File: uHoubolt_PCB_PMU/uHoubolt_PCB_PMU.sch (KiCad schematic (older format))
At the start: 43 parts, among them J1 Conn_01x04, J2 Conn_01x02, J3 Conn_01x04, Q1 BUK7M27-80EX, Q2 Si7141DP, SW1 SW_Push_SPDT, SW2 SW_Push_SPDT, U1 INA226, U2 MAX1873SEEE

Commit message: replace mosfet
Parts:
- removed Q1: BUK7M27-80EX, Package_TO_SOT_SMD:LFPAK33, symbol Transistor_FET:BUK7M27-80EX
- added Q?: ZXMN3F30FH, Package_TO_SOT_SMD:SOT-23, symbol Transistor_FET:ZXMN3F30FH
- added R?: 200, symbol Device:R_Small
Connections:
- wire segments 149 -> 151
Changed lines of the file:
@@
 Wire Wire Line
 	6700 4350 6700 4500
-$Comp
-L power:GND #PWR016
-U 1 1 5FE435F1
-P 6700 4700
-F 0 "#PWR016" H 6700 4450 50  0001 C CNN
-F 1 "GND" H 6705 4527 50  0000 C CNN
-F 2 "" H 6700 4700 50  0001 C CNN
-F 3 "" H 6700 4700 50  0001 C CNN
-	1    6700 4700
-	1    0    0    -1
-$EndComp
 Wire Wire Line
 	6550 4000 6550 3800
@@
 	1    0    0    1
 $EndComp
-$Comp
-L Transistor_FET:BUK7M27-80EX Q1
-U 1 1 600D7062
-P 5950 3850
-F 0 "Q1" H 5650 3750 50  0000 L CNN
-F 1 "BUK7M27-80EX" H 5400 3650 50  0000 L CNN
-F 2 "Package_TO_SOT_SMD:LFPAK33" H 6150 3775 50  0001 L CIN
-F 3 "https://assets.nexperia.com/documents/data-sheet/BUK7M27-80E.pdf" V 5950 3850 50  0001 L CNN
-	1    5950 3850
-	1    0    0    -1
-$EndComp
-Text Label 5400 3850 0    50   ~ 0
+Text Label 5175 3850 0    50   ~ 0
 DISABLE
-Wire Wire Line
-	5400 3850 5750 3850
 Wire Wire Line
 	6050 3650 6700 3650
@@
 	6700 3650 6700 3700
 Connection ~ 6700 3700
-$Comp
-L power:GND #PWR013
-U 1 1 600E6257
-P 6050 4050
-F 0 "#PWR013" H 6050 3800 50  0001 C CNN
-F 1 "GND" H 6125 3875 50  0000 R CNN
-F 2 "" H 6050 4050 50  0001 C CNN
-F 3 "" H 6050 4050 50  0001 C CNN
-	1    6050 4050
-	1    0    0    -1
-$EndComp
 $Comp
 L Device:R_Small R14
@@
 Wire Wire Line
 	3400 5450 3000 5450
+$Comp
+L Transistor_FET:ZXMN3F30FH Q?
+U 1 1 5FF6F840
+P 5950 3850
+F 0 "Q?" H 6154 3896 50  0000 L CNN
+F 1 "ZXMN3F30FH" H 6154 3805 50  0000 L CNN
+F 2 "Package_TO_SOT_SMD:SOT-23" H 6150 3775 50  0001 L CIN
+F 3 "http://www.diodes.com/assets/Datasheets/ZXMN3F30FH.pdf" H 5950 3850 50  0001 L CNN
+	1    5950 3850
+	1    0    0    -1
+$EndComp
+$Comp
+L power:GND #PWR016
+U 1 1 5FE435F1
+P 6700 4700
+F 0 "#PWR016" H 6700 4450 50  0001 C CNN
+F 1 "GND" H 6705 4527 50  0000 C CNN
+F 2 "" H 6700 4700 50  0001 C CNN
+F 3 "" H 6700 4700 50  0001 C CNN
+	1    6700 4700
+	1    0    0    -1
+$EndComp
+$Comp
+L power:GND #PWR?
+U 1 1 5FF780F7
+P 6050 4100
+F 0 "#PWR?" H 6050 3850 50  0001 C CNN
+F 1 "GND" H 6055 3927 50  0000 C CNN
+F 2 "" H 6050 4100 50  0001 C CNN
+F 3 "" H 6050 4100 50  0001 C CNN
+	1    6050 4100
+	1    0    0    -1
+$EndComp
+Wire Wire Line
+	6050 4050 6050 4100
+$Comp
+L Device:R_Small R?
+U 1 1 5FF7FCD0
+P 5550 3850
+F 0 "R?" V 5625 3800 50  0000 L CNN
+F 1 "200" V 5675 3775 50  0000 L CNN
+F 2 "" H 5550 3850 50  0001 C CNN
+F 3 "~" H 5550 3850 50  0001 C CNN
+	1    5550 3850
+	0    1    1    0
+$EndComp
+Wire Wire Line
+	5650 3850 5750 3850
+Wire Wire Line
+	5450 3850 5175 3850
 $EndSCHEMATC

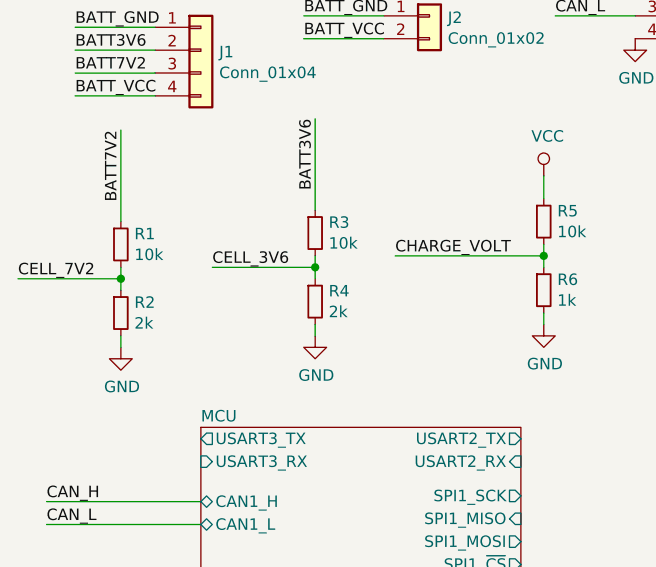
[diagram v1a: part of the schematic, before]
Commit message: change voltage divider values
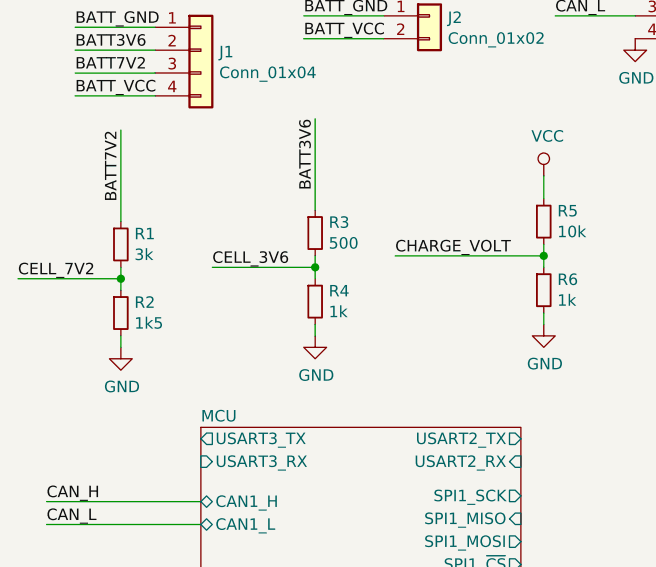
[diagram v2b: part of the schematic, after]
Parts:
- R1: value 10k -> 3k
- R2: value 2k -> 1k5
- R3: value 10k -> 500
- R4: value 2k -> 1k
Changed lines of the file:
@@
 AR Path="/5FE7A048" Ref="R3"  Part="1"
 F 0 "R3" H 2159 2946 50  0000 L CNN
-F 1 "10k" H 2159 2855 50  0000 L CNN
+F 1 "500" H 2159 2855 50  0000 L CNN
 F 2 "" H 2100 2900 50  0001 C CNN
 F 3 "~" H 2100 2900 50  0001 C CNN
@@
 AR Path="/5FE7A04E" Ref="R4"  Part="1"
 F 0 "R4" H 2159 3246 50  0000 L CNN
-F 1 "2k" H 2159 3155 50  0000 L CNN
+F 1 "1k" H 2159 3155 50  0000 L CNN
 F 2 "" H 2100 3200 50  0001 C CNN
 F 3 "~" H 2100 3200 50  0001 C CNN
@@
 AR Path="/5FE86386" Ref="R1"  Part="1"
 F 0 "R1" H 1309 2996 50  0000 L CNN
-F 1 "10k" H 1309 2905 50  0000 L CNN
+F 1 "3k" H 1309 2905 50  0000 L CNN
 F 2 "" H 1250 2950 50  0001 C CNN
 F 3 "~" H 1250 2950 50  0001 C CNN
@@
 AR Path="/5FE8638C" Ref="R2"  Part="1"
 F 0 "R2" H 1309 3296 50  0000 L CNN
-F 1 "2k" H 1309 3205 50  0000 L CNN
+F 1 "1k5" H 1309 3205 50  0000 L CNN
 F 2 "" H 1250 3250 50  0001 C CNN
 F 3 "~" H 1250 3250 50  0001 C CNN

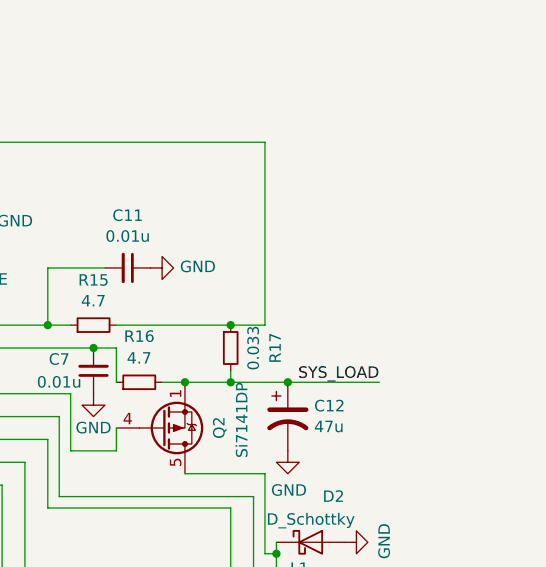
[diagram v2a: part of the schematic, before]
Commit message: add voltage divider sys_load
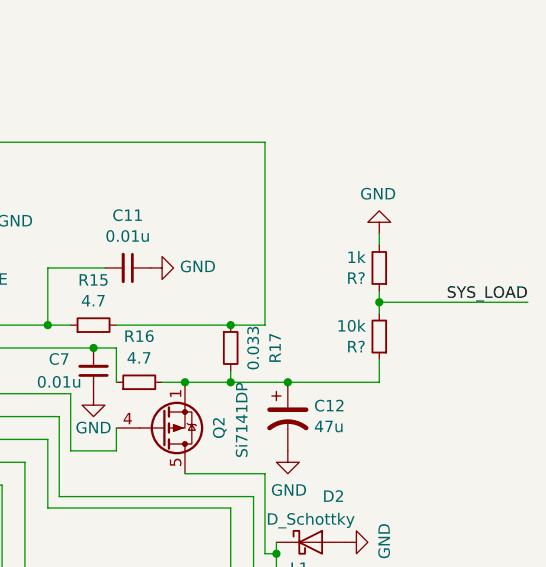
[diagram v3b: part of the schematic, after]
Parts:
- added R?: 10k, symbol Device:R_Small
- added R?: 1k, symbol Device:R_Small
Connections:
- net GND: now also R?.2
- net SYS_LOAD: now also R?.1, R?.2; no longer C12.1, Q2.1 (S), Q2.2 (S), Q2.3 (S), R16.2, R17.2
- new net: C12.1, Q2.1 (S), Q2.2 (S), Q2.3 (S), R16.2, R17.2, R?.1
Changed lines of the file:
@@
 	9400 3650 9650 3650
 Connection ~ 9400 3650
-Text Label 10050 3650 2    50   ~ 0
+Text Label 10700 3300 2    50   ~ 0
 SYS_LOAD
 Wire Wire Line
@@
 Wire Wire Line
 	5450 3850 5175 3850
+$Comp
+L Device:R_Small R?
+U 1 1 5FF91AB4
+P 10050 3450
+AR Path="/6016029C/5FF91AB4" Ref="R?"  Part="1"
+AR Path="/5FF91AB4" Ref="R?"  Part="1"
+F 0 "R?" H 10109 3496 50  0000 L CNN
+F 1 "10k" H 10109 3405 50  0000 L CNN
+F 2 "" H 10050 3450 50  0001 C CNN
+F 3 "~" H 10050 3450 50  0001 C CNN
+	1    10050 3450
+	-1   0    0    1
+$EndComp
+$Comp
+L Device:R_Small R?
+U 1 1 5FF91ABA
+P 10050 3150
+AR Path="/6016029C/5FF91ABA" Ref="R?"  Part="1"
+AR Path="/5FF91ABA" Ref="R?"  Part="1"
+F 0 "R?" H 10109 3196 50  0000 L CNN
+F 1 "1k" H 10109 3105 50  0000 L CNN
+F 2 "" H 10050 3150 50  0001 C CNN
+F 3 "~" H 10050 3150 50  0001 C CNN
+	1    10050 3150
+	-1   0    0    1
+$EndComp
+$Comp
+L power:GND #PWR?
+U 1 1 5FF91AC0
+P 10050 3000
+AR Path="/6016029C/5FF91AC0" Ref="#PWR?"  Part="1"
+AR Path="/5FF91AC0" Ref="#PWR?"  Part="1"
+F 0 "#PWR?" H 10050 2750 50  0001 C CNN
+F 1 "GND" H 10055 2827 50  0000 C CNN
+F 2 "" H 10050 3000 50  0001 C CNN
+F 3 "" H 10050 3000 50  0001 C CNN
+	1    10050 3000
+	-1   0    0    1
+$EndComp
+Wire Wire Line
+	10050 3300 10050 3250
+Wire Wire Line
+	10050 3350 10050 3300
+Connection ~ 10050 3300
+Wire Wire Line
+	10050 3650 10050 3550
+Wire Wire Line
+	10050 3000 10050 3050
+Wire Wire Line
+	10700 3300 10050 3300
 $EndSCHEMATC

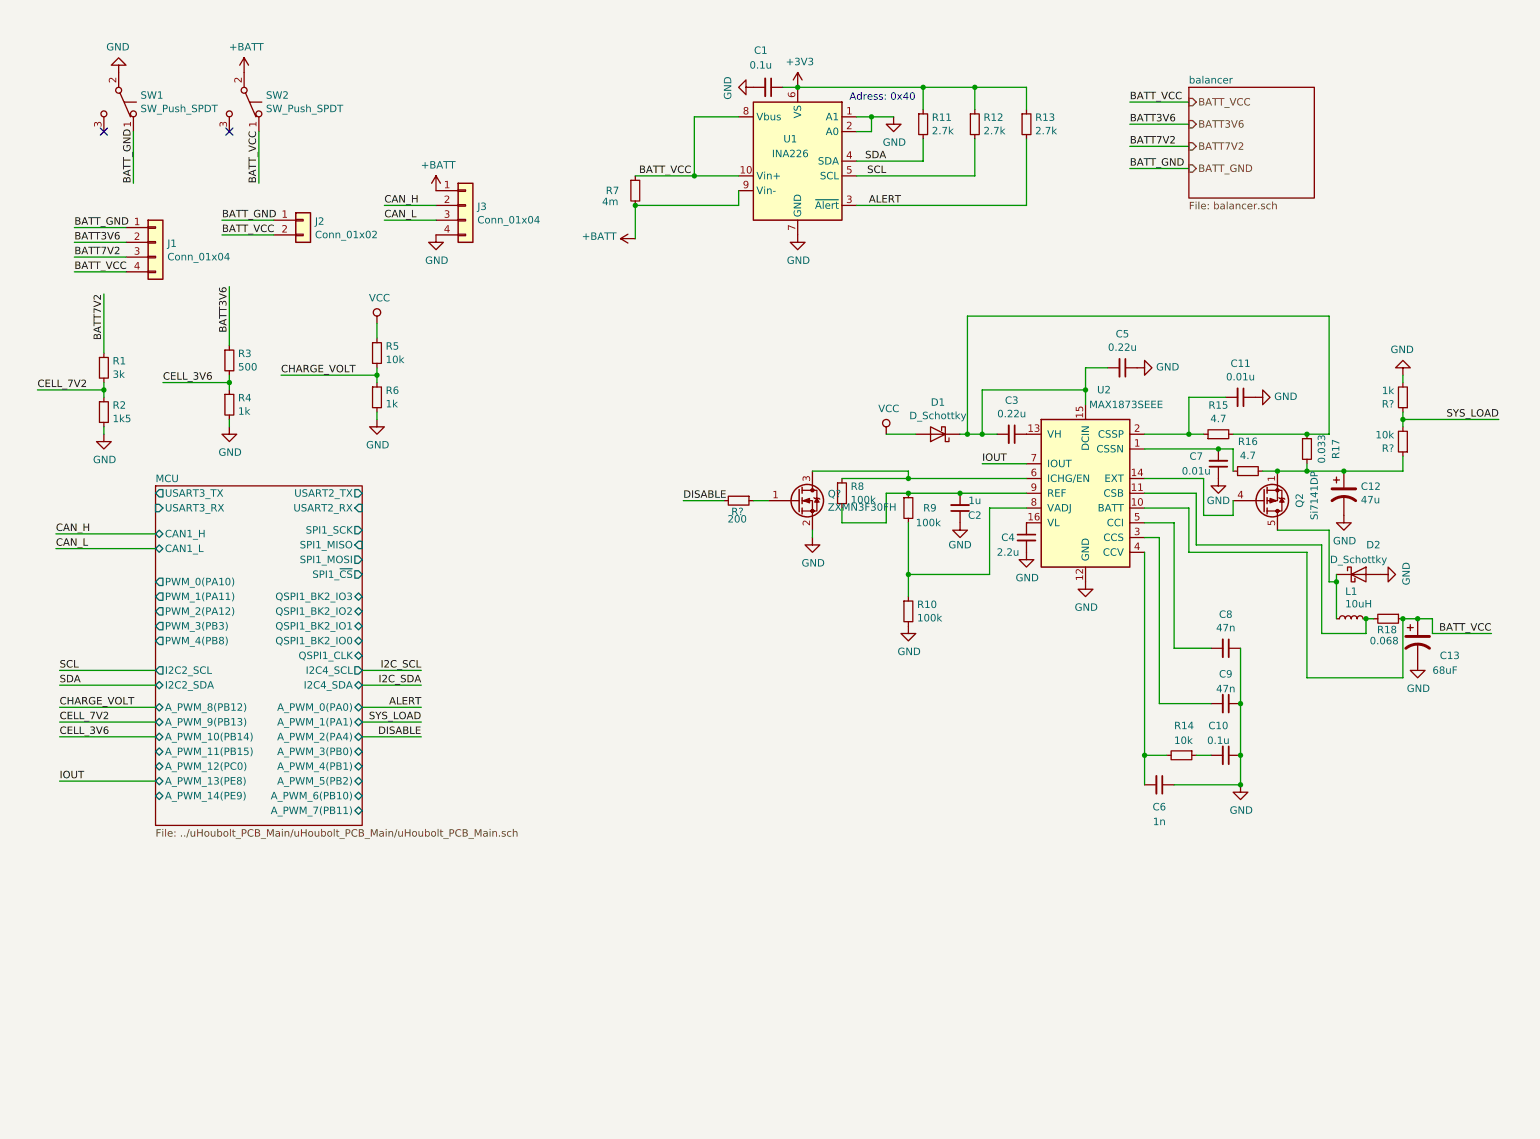
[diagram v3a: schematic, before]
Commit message: bat+ lable change, change mosfets balancer, remove sys_load
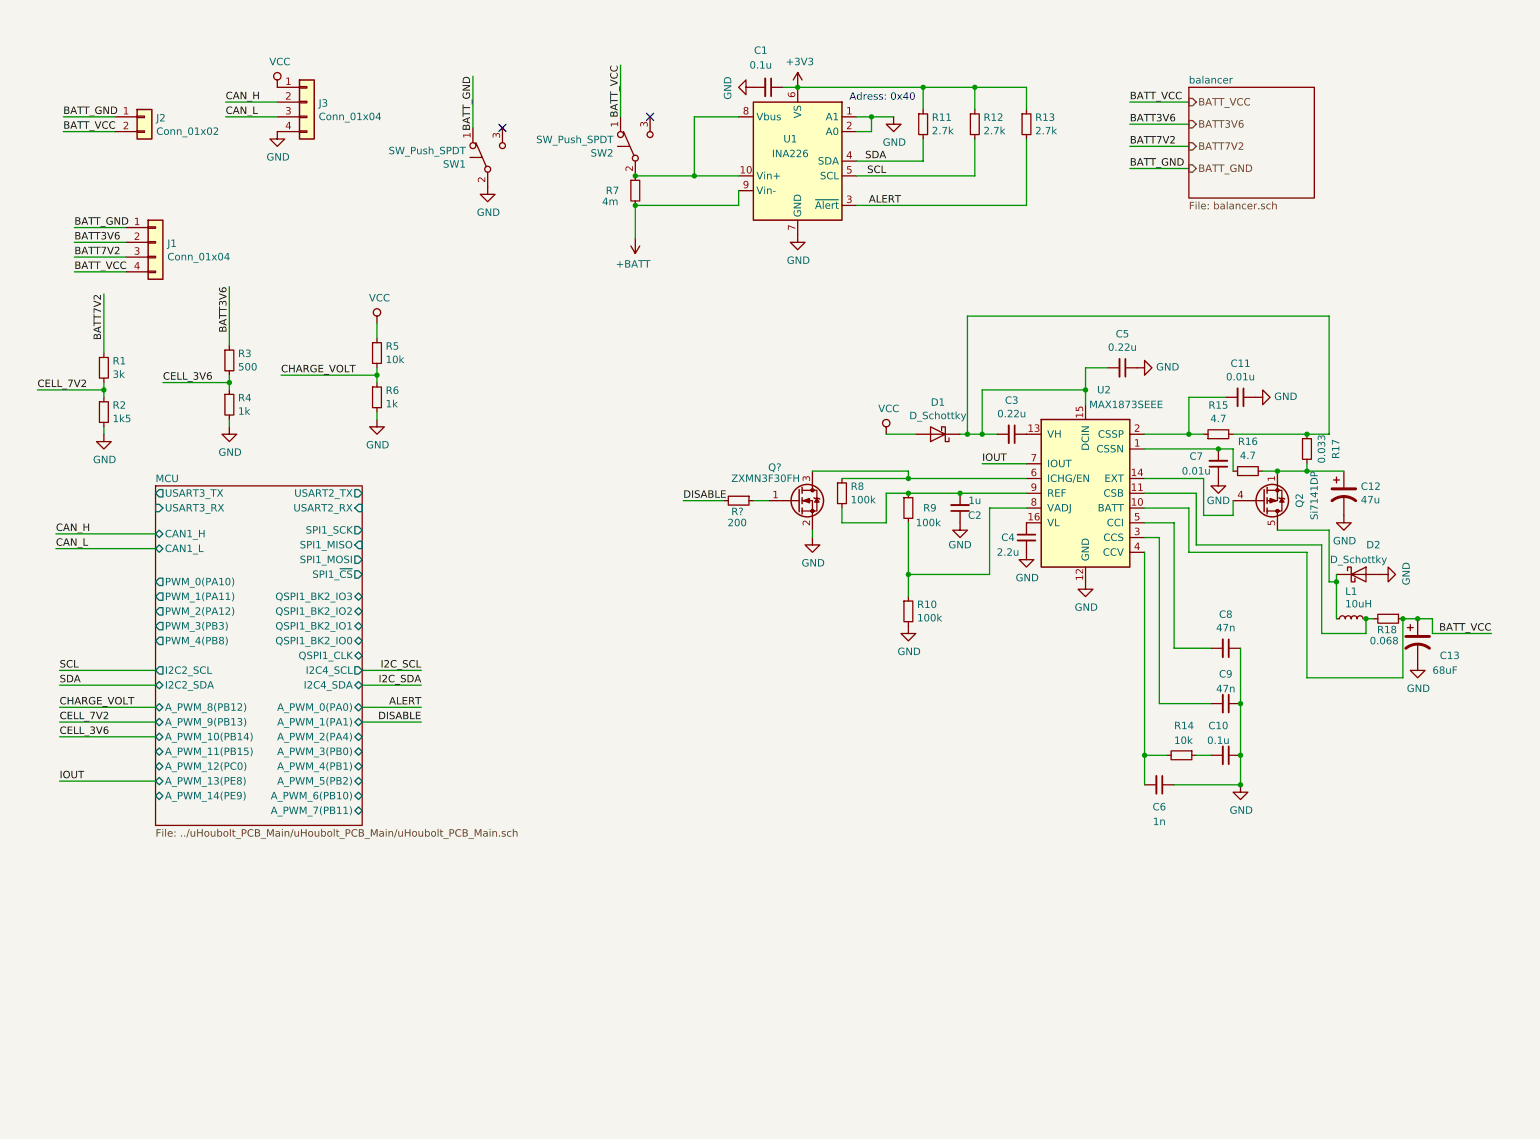
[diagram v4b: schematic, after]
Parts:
- removed R?: 10k, symbol Device:R_Small
- removed R?: 1k, symbol Device:R_Small
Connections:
- net +BATT: no longer J3.1 (Pin_1), SW2.2 (B)
- net BATT_VCC: no longer R7.1, U1.10 (Vin+), U1.8 (Vbus)
- net VCC: now also J3.1 (Pin_1)
- new net: R7.1, SW2.2 (B), U1.10 (Vin+), U1.8 (Vbus)
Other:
- moved on the sheet: J2, J3, SW1, SW2

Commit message: Add descriptions
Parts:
- gave numbers to parts that had none: 2
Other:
- note added: "Balancer"
- note added: "Cell Voltage Measurements\n"
- note added: "Charger Controller"
- note added: "Current Measurement"
- moved on the sheet: J1, J2, J3, R3, R4, R5, R6

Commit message: change description
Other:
- note added: "Current/Voltage Measurement"
- note removed: "Current Measurement"
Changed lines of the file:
@@
 Wire Notes Line
 	4100 550  4100 2325
-Text Notes 6600 725  0    79   ~ 0
-Current Measurement
+Text Notes 6075 675  0    79   ~ 0
+Current/Voltage Measurement
 Wire Notes Line
 	650  2375 3800 2375
